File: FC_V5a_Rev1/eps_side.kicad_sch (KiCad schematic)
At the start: 71 parts, among them CN1 DF13C-5P-1.25V(21), CN2 DF13C-5P-1.25V(21), CN3 DF13C-5P-1.25V(21), CN4 DF13C-5P-1.25V(21), IC6 LT3652IMSE#PBF, J10 INHIBIT_P2, J13 Bypass, J14 Battery Input, J17 Face4 (Z- Face), J19 ISS_INHIBIT, J20 RBF_Inhibit, J21 Heater Output, J29 INHIBIT_S2, J7 INHIBIT_P1, J8 INHIBIT_S1, U10 TPS54226PWPRPWP14_2P31X2P46-L, U13 TPS7A4501DCQT, U14 INA219AxD, U15 INA219AxD, U17 LMC555CMX/NOPB, U20 74LVC1G04, U9 MCP23017_SS

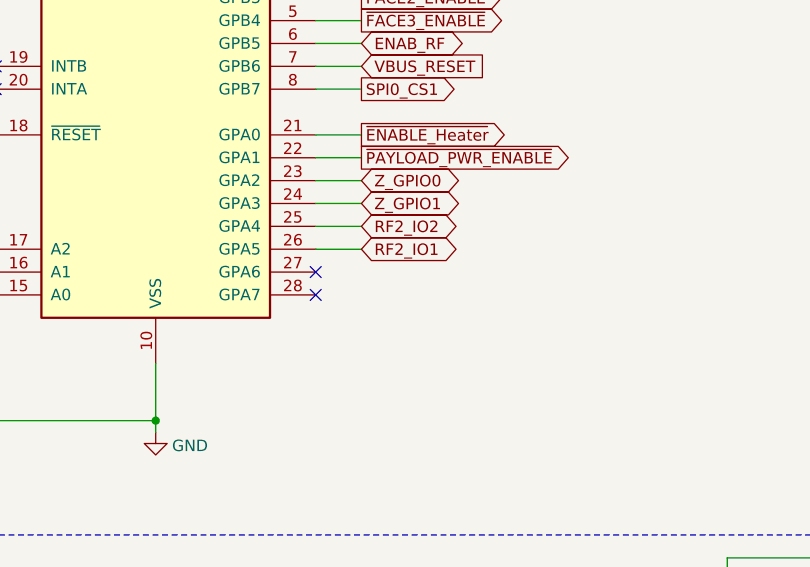
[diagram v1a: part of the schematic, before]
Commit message: Added CHRG and READONLY Sensing to GPIO Expander
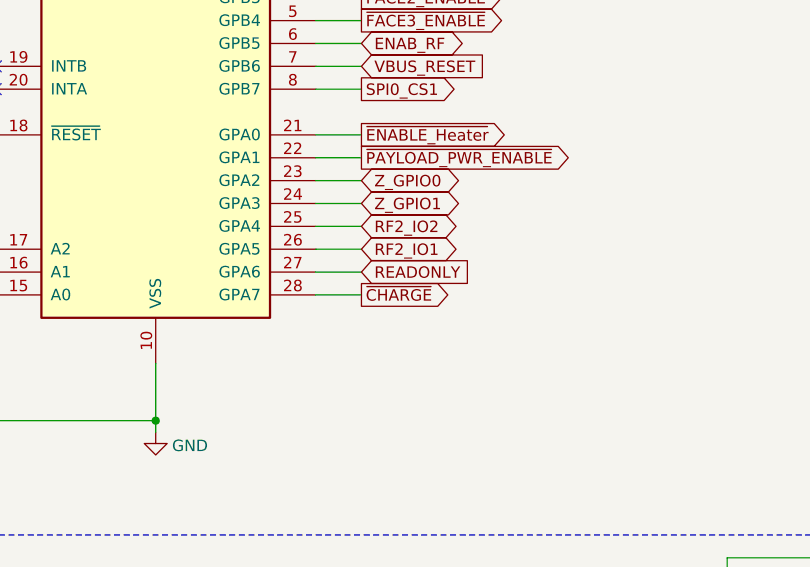
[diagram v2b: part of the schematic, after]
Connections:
- net ~{CHARGE}: now also U9.28 (GPA7)
- net READONLY: now reaches U9.27 (GPA6)
- no-connect marks 6 -> 4
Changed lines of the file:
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@@
 	)
 	(no_connect
-		(at 92.71 199.39)
-	)
-	(no_connect
 		(at 57.15 176.53)
 	)
@@
 	)
 	(no_connect
-		(at 92.71 196.85)
-	)
-	(no_connect
 		(at 57.15 173.99)
 	)
@@
 	(wire
 		(pts
+			(xy 92.71 199.39) (xy 97.79 199.39)
+		)
+		(stroke
+			(width 0)
+			(type default)
+		)
+	)
+	(wire
+		(pts
 			(xy 281.94 81.28) (xy 281.94 78.74)
 		)
@@
 	(wire
 		(pts
+			(xy 92.71 196.85) (xy 97.79 196.85)
+		)
+		(stroke
+			(width 0)
+			(type default)
+		)
+	)
+	(wire
+		(pts
 			(xy 142.24 64.77) (xy 142.24 52.07)
 		)
@@
 		)
 	)
+	(global_label "~{CHARGE}"
+		(shape output)
+		(at 97.79 199.39 0)
+		(fields_autoplaced yes)
+		(effects
+			(font
+				(size 1.27 1.27)
+			)
+			(justify left)
+		)
+		(property "Intersheetrefs" "${INTERSHEET_REFS}"
+			(at 108.1533 199.39 0)
+			(effects
+				(font
+					(size 1.27 1.27)
+				)
+				(justify left)
+				(hide yes)
+			)
+		)
+	)
 	(global_label "V_RBF"
 		(shape bidirectional)
@@
 			(effects
 				(font
+					(size 1.27 1.27)
+				)
+				(justify left)
+				(hide yes)
+			)
+		)
+	)
+	(global_label "READONLY"
+		(shape input)
+		(at 97.79 196.85 0)
+		(fields_autoplaced yes)
+		(effects
+			(font
+				(size 1.27 1.27)
+			)
+			(justify left)
+		)
+		(property "Intersheetrefs" "${INTERSHEET_REFS}"
+			(at 110.3305 196.85 0)
+			(effects
+				(font

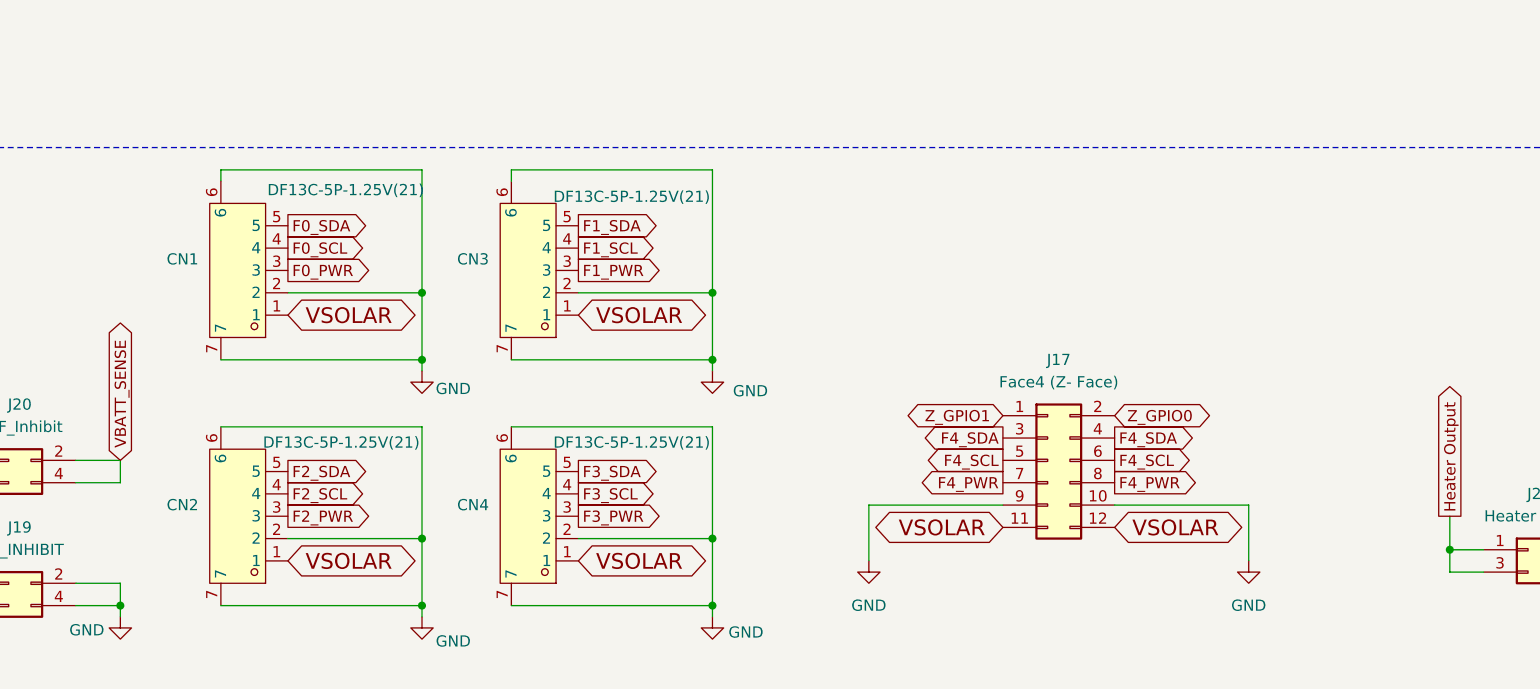
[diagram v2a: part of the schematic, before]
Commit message: Replaced DF13s with DF11s
Going from 4x 5pos DF13 to 2x 12pos DF11 Surface Mount Connectors
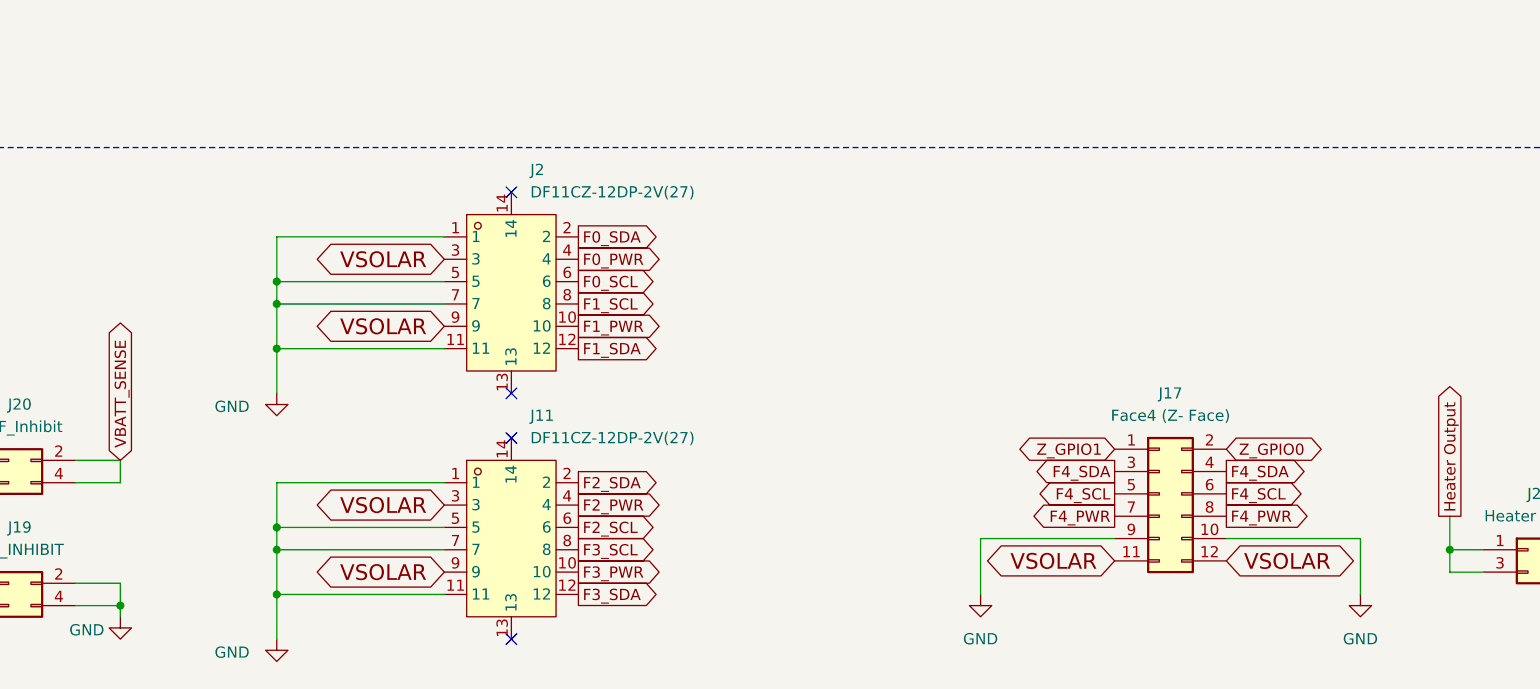
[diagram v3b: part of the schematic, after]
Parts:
- removed CN1, CN2, CN3, CN4: DF13C-5P-1.25V(21), easyeda2kicad:CONN-SMD_DF13C-5P-1.25V-21, symbol easyeda2kicad:DF13C-5P-1.25V(21)
- added J11, J2: DF11CZ-12DP-2V(27), easyeda2kicad:CONN-SMD_12P-P2.00_DF11CZ-12DP, symbol easyeda2kicad:DF11CZ-12DP-2V(27)
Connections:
- net F0_PWR: now also J2.4
- net F0_SCL: now also J2.6
- net F0_SDA: now also J2.2
- net F1_PWR: now also J2.10
- net F1_SCL: now also J2.8
- net F1_SDA: now also J2.12
- net F2_PWR: now also J11.4
- net F2_SCL: now also J11.6
- net F2_SDA: now also J11.2
- net F3_PWR: now also J11.10
- net F3_SCL: now also J11.8
- net F3_SDA: now also J11.12
- net GND: now also J11.1, J11.11, J11.5, J11.7, J2.1, J2.11, J2.5, J2.7
- net VSOLAR: now also J11.3, J11.9, J2.3, J2.9
- no-connect marks 4 -> 8
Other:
- moved on the sheet: J17
